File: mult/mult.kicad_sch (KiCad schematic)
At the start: 0 parts

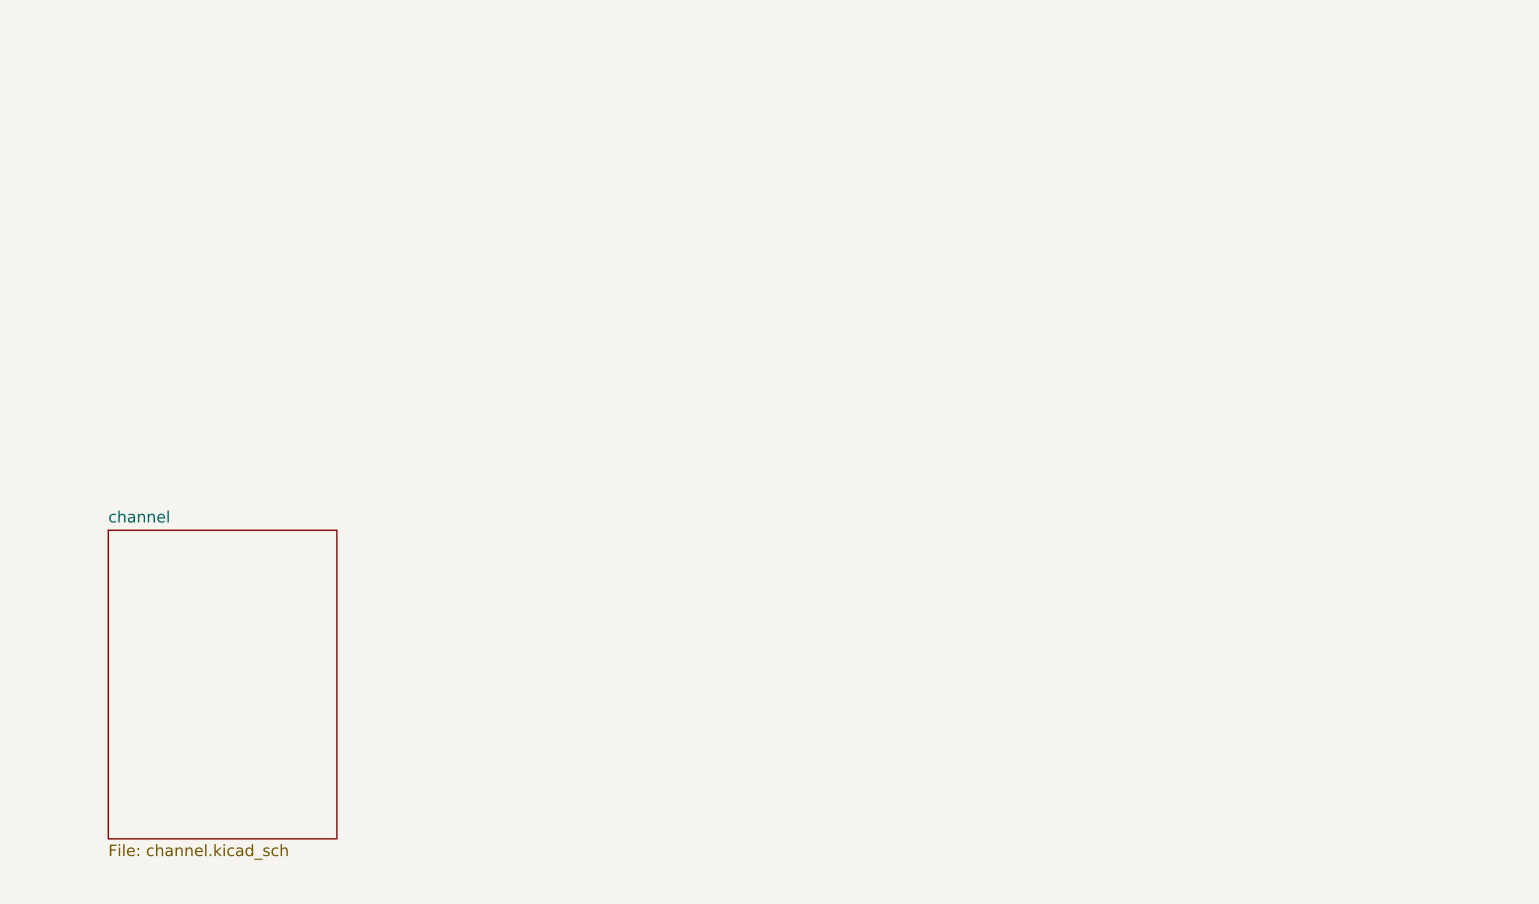
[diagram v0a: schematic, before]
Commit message: mult: Populate root schematic, add LEDs
Placeholder Eurorack_Power is placed but missing diode + caps. Should
probably be replaced with reusable power subschematic.
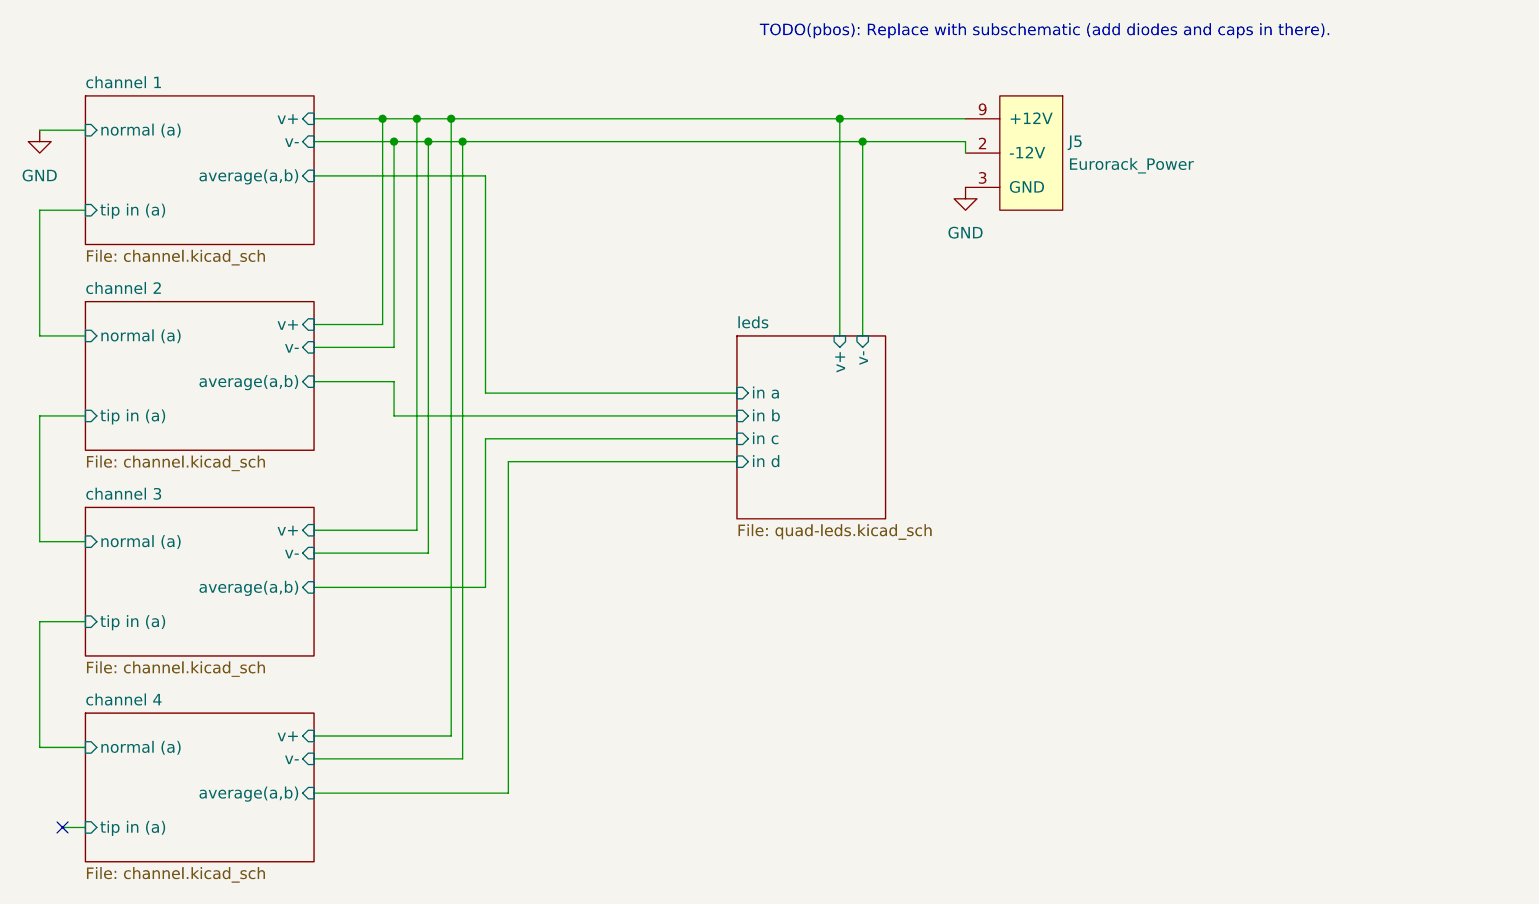
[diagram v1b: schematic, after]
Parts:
- added J5: Eurorack_Power, winterbloom:Eurorack_Power_2x5_Shrouded, symbol winterbloom:Eurorack_Power
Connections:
- new net GND: J5.3 (GND), J5.4 (GND), J5.5 (GND), J5.6 (GND), J5.7 (GND), J5.8 (GND)
- new net channel 1/v+: J5.10 (+12V), J5.9 (+12V)
- new net channel 1/v-: J5.1 (-12V), J5.2 (-12V)
- no-connect marks 0 -> 1
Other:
- sheet channel renamed channel 1
- added sheet channel 2 (channel.kicad_sch)
- added sheet channel 3 (channel.kicad_sch)
- added sheet channel 4 (channel.kicad_sch)
- added sheet leds (quad-leds.kicad_sch)
- sheet channel 1 ports: added average(a,b), normal (a), tip in (a), v+, v-; removed none
- note added: "TODO(pbos): Replace with subschematic (add diodes and caps in there)."

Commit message: mult: Replace v+ and v- labels with VCC,VEE
This removes a lot of unnecessary wires as well. Also updating LED
resistors to 1k to match Mutable Instruments Links and resolving TODO.
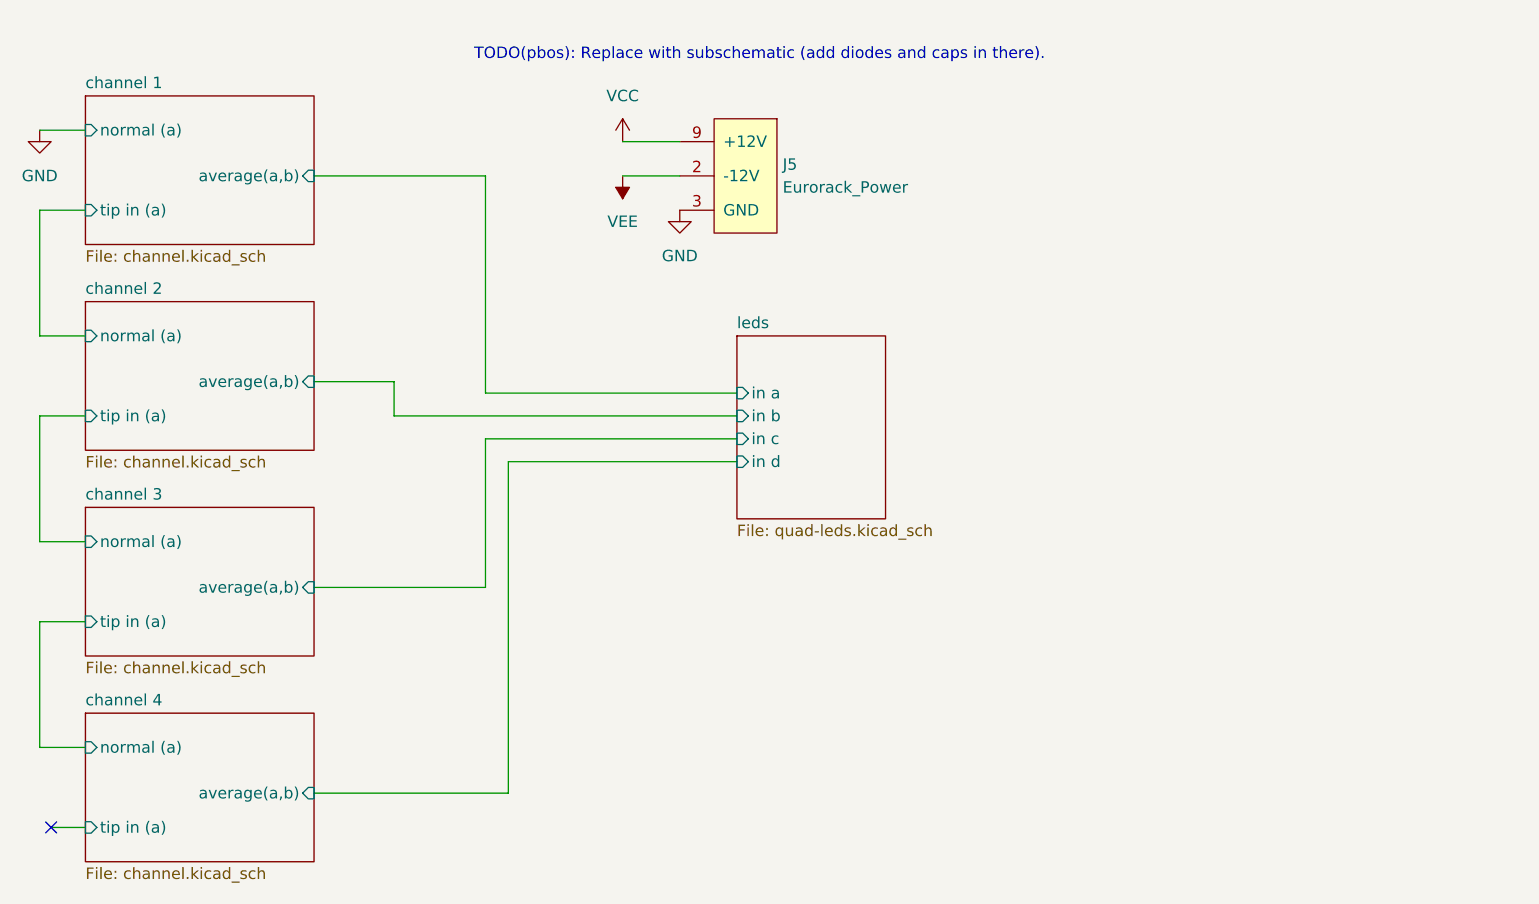
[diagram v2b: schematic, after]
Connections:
- net channel 1/v+ renamed VCC
- net channel 1/v- renamed VEE
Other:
- sheet channel 1 ports: added none; removed v+, v-
- sheet channel 2 ports: added none; removed v+, v-
- sheet channel 3 ports: added none; removed v+, v-
- sheet channel 4 ports: added none; removed v+, v-
- sheet leds ports: added none; removed v+, v-
- moved on the sheet: J5

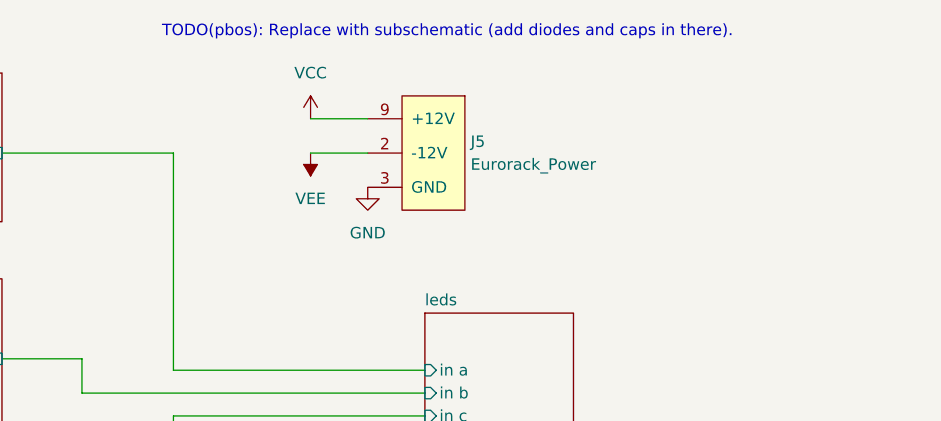
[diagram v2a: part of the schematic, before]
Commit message: mult: Add power subschematic
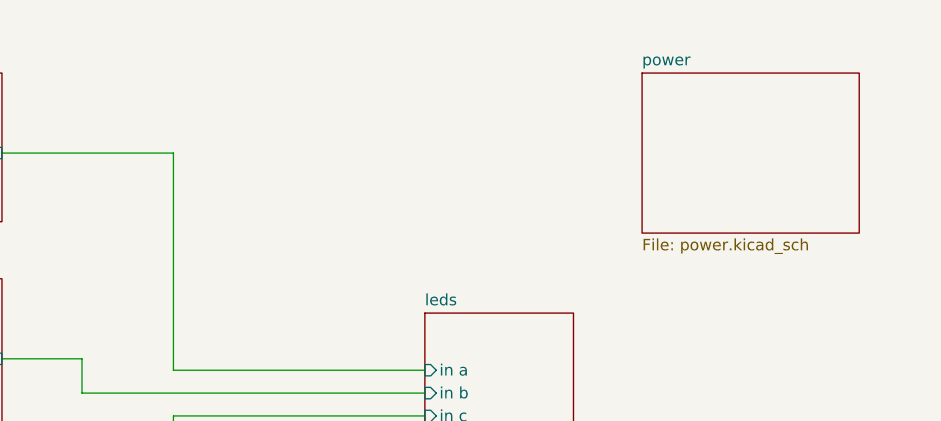
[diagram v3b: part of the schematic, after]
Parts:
- removed J5: Eurorack_Power, winterbloom:Eurorack_Power_2x5_Shrouded, symbol winterbloom:Eurorack_Power
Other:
- added sheet power (power.kicad_sch)
- note removed: "TODO(pbos): Replace with subschematic (add diodes and caps in there)."
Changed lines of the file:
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@@
-    (stroke (width 0) (type default))
-  )
-  (wire (pts (xy 120.65 53.34) (xy 127 53.34))
     (stroke (width 0) (type default))
   )
@@
   )
   (wire (pts (xy 133.35 80.01) (xy 95.25 80.01))
-    (stroke (width 0) (type default))
-  )
-  (wire (pts (xy 120.65 49.53) (xy 127 49.53))
     (stroke (width 0) (type default))
   )
@@
     (stroke (width 0) (type default))
   )
-  (text "TODO(pbos): Replace with subschematic (add diodes and caps in there)."
-    (at 104.14 40.64 0)
-    (effects (font (size 1.27 1.27)) (justify left bottom))
-  )
   (symbol (lib_id "power:GND") (at 55.88 48.26 0) (unit 1)
     (in_bom yes) (on_board yes) (dnp no) (fields_autoplaced)
@@
         (path "/0e98ec4b-b4c7-447c-abd7-a761177a7f67"
           (reference "#PWR037") (unit 1)
-        )
-      )
-    )
-  )
-  (symbol (lib_id "winterbloom:Eurorack_Power") (at 134.62 53.34 0) (mirror y) (unit 1)
-    (in_bom yes) (on_board yes) (dnp no) (fields_autoplaced)
-    (property "Reference" "J5" (at 138.43 52.07 0)
-      (effects (font (size 1.27 1.27)) (justify right))
-    )
-    (property "Value" "Eurorack_Power" (at 138.43 54.61 0)
-      (effects (font (size 1.27 1.27)) (justify right))
-    )
-    (property "Footprint" "winterbloom:Eurorack_Power_2x5_Shrouded" (at 134.62 41.91 0)
-      (effects (font (size 1.27 1.27)) hide)
-    )
-    (property "Datasheet" "https://static6.arrow.com/aropdfconversion/1507f1621f4e67855dd466ebb3ac550d52564a9d/32302-sxx1.pdf" (at 133.985 66.675 0)
-      (effects (font (size 1.27 1.27)) hide)
-    )
-    (property "MPN" "302-S101" (at 134.62 39.37 0)
-      (effects (font (size 1.27 1.27)) hide)
-    )
-    (pin "1")
-    (pin "10")
-    (pin "2")
-    (pin "3")
-    (pin "4")
-    (pin "5")
-    (pin "6")
-    (pin "7")
-    (pin "8")
-    (pin "9")
-    (instances
-      (project "mult"
-        (path "/0e98ec4b-b4c7-447c-abd7-a761177a7f67"
-          (reference "J5") (unit 1)
-        )
-      )
-    )
-  )
-  (symbol (lib_id "power:VEE") (at 120.65 53.34 180) (unit 1)
-    (in_bom yes) (on_board yes) (dnp no) (fields_autoplaced)
-    (property "Reference" "#PWR055" (at 120.65 49.53 0)
-      (effects (font (size 1.27 1.27)) hide)
-    )
-    (property "Value" "VEE" (at 120.65 58.42 0)
-      (effects (font (size 1.27 1.27)))
-    )
-    (property "Footprint" "" (at 120.65 53.34 0)
-      (effects (font (size 1.27 1.27)) hide)
-    )
-    (property "Datasheet" "" (at 120.65 53.34 0)
-      (effects (font (size 1.27 1.27)) hide)
-    )
-    (pin "1")
-    (instances
-      (project "mult"
-        (path "/0e98ec4b-b4c7-447c-abd7-a761177a7f67"
-          (reference "#PWR055") (unit 1)
-        )
-      )
-    )
-  )
-  (symbol (lib_id "power:GND") (at 127 57.15 0) (unit 1)
-    (in_bom yes) (on_board yes) (dnp no) (fields_autoplaced)
-    (property "Reference" "#PWR010" (at 127 63.5 0)
-      (effects (font (size 1.27 1.27)) hide)
-    )
-    (property "Value" "GND" (at 127 62.23 0)
-      (effects (font (size 1.27 1.27)))
-    )
-    (property "Footprint" "" (at 127 57.15 0)
-      (effects (font (size 1.27 1.27)) hide)
-    )
-    (property "Datasheet" "" (at 127 57.15 0)
-      (effects (font (size 1.27 1.27)) hide)
-    )
-    (pin "1")
-    (instances
-      (project "mult"
-        (path "/0e98ec4b-b4c7-447c-abd7-a761177a7f67"
-          (reference "#PWR010") (unit 1)
-        )
-      )
-    )
-  )
-  (symbol (lib_id "power:VCC") (at 120.65 49.53 0) (unit 1)
-    (in_bom yes) (on_board yes) (dnp no) (fields_autoplaced)
-    (property "Reference" "#PWR056" (at 120.65 53.34 0)
-      (effects (font (size 1.27 1.27)) hide)
-    )
-    (property "Value" "VCC" (at 120.65 44.45 0)
-      (effects (font (size 1.27 1.27)))
-    )
-    (property "Footprint" "" (at 120.65 49.53 0)
-      (effects (font (size 1.27 1.27)) hide)
-    )
-    (property "Datasheet" "" (at 120.65 49.53 0)
-      (effects (font (size 1.27 1.27)) hide)
-    )
-    (pin "1")
-    (instances
-      (project "mult"
-        (path "/0e98ec4b-b4c7-447c-abd7-a761177a7f67"
-          (reference "#PWR056") (unit 1)
         )
       )
@@
       )
     )
+  )
+  (sheet (at 157.48 44.45) (size 24.13 17.78) (fields_autoplaced)
+    (stroke (width 0.1524) (type solid))
+    (fill (color 0 0 0 0.0000))
+    (property "Sheetname" "power" (at 157.48 43.7384 0)
+      (effects (font (size 1.27 1.27)) (justify left bottom))
+    )
+    (property "Sheetfile" "power.kicad_sch" (at 157.48 62.8146 0)
+      (effects (font (size 1.27 1.27)) (justify left top))
+    )
+    (instances
+      (project "mult"
+        (path "/0e98ec4b-b4c7-447c-abd7-a761177a7f67" (page "7"))
+      )
+    )
